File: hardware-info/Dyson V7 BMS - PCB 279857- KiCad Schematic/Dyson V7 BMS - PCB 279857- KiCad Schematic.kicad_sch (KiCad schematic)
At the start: 109 parts, among them P5 OUT-, Q1 BC856A, Q2 BC817-25, Q3 PSMN0R9-30ULD, Q4 PMV45EN2, Q5 PMV45EN2, U1 PIC16LF1847, U2 ISL94208, U3 MCP1525-TT, U4 Conn_02x04_Counter_Clockwise

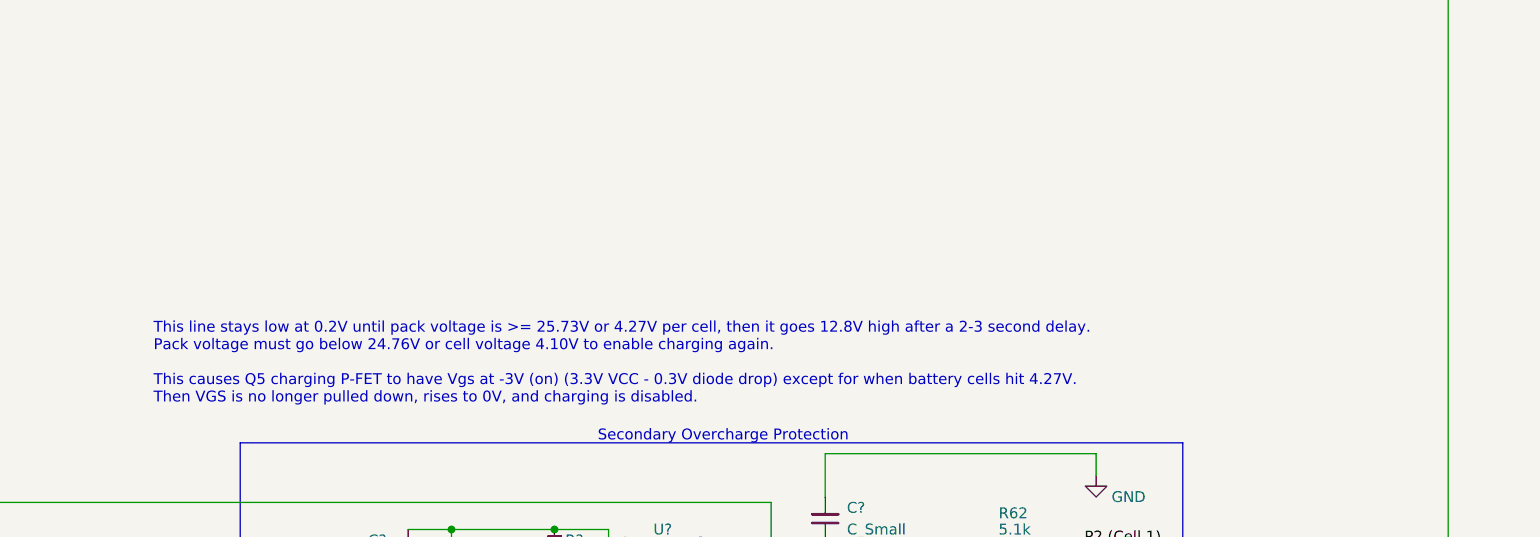
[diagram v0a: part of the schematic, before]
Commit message: Added over-charge protection IC info to V7 schematic
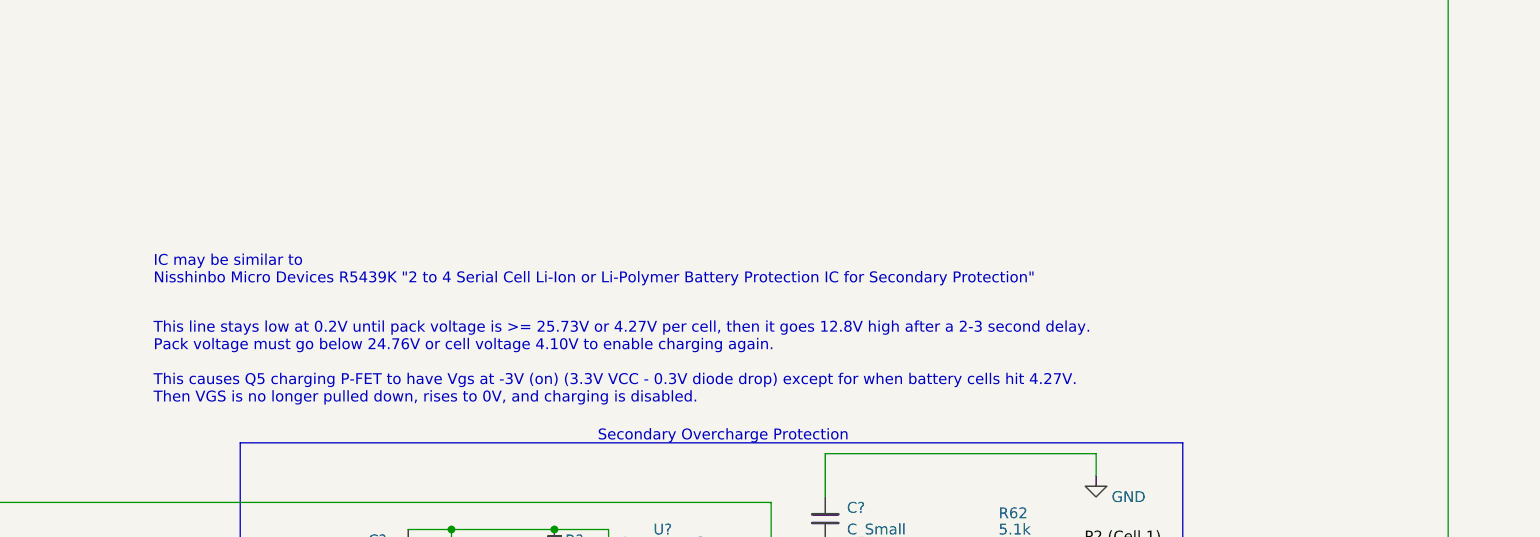
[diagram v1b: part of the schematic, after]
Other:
- note added: "IC may be similar to Nisshinbo Micro Devices R5439K "2 to 4 Serial Cell Li-Ion or Li-Polymer Battery Protection IC for Secondary Protection""
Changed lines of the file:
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@@
   (title_block
     (title "Dyson V7 BMS - PCB 279857")
-    (date "2022-05-11")
-    (rev "1.0")
+    (date "2022-05-16")
+    (rev "1.01")
     (company "tinfever")
     (comment 1 "See COPYING for license")
@@
     (effects (font (size 1.27 1.27)) (justify left bottom))
   )
+  (text "IC may be similar to\nNisshinbo Micro Devices R5439K \"2 to 4 Serial Cell Li-Ion or Li-Polymer Battery Protection IC for Secondary Protection\""
+    (at 241.935 165.1 0)
+    (effects (font (size 1.27 1.27)) (justify left bottom))
+  )
